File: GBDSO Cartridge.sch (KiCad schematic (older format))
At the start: 75 parts, among them J1 MJ-3523-SMT-TR, J2 MJ-3523-SMT-TR, J3 EdgeConnector, J5 Conn_01x02, J6 Conn_01x02, P1 100k, P2 100k, SW1 SW_SPDT, SW2 SW_SPDT, U1 TL072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

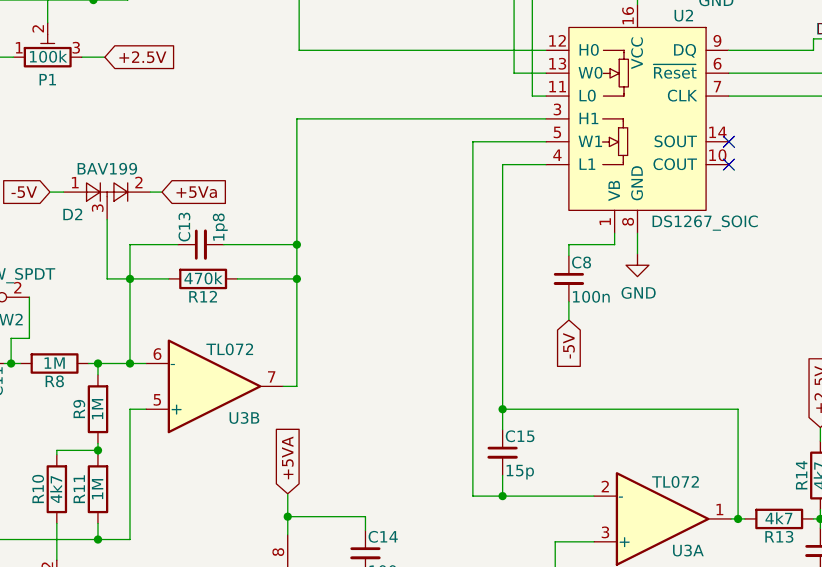
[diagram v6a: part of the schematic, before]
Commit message: issue #16, #17 and #18 are fixed in the schematic but not yet in the PCB
reopened issue #16 and #17 as they were not yet fixed in the PCB
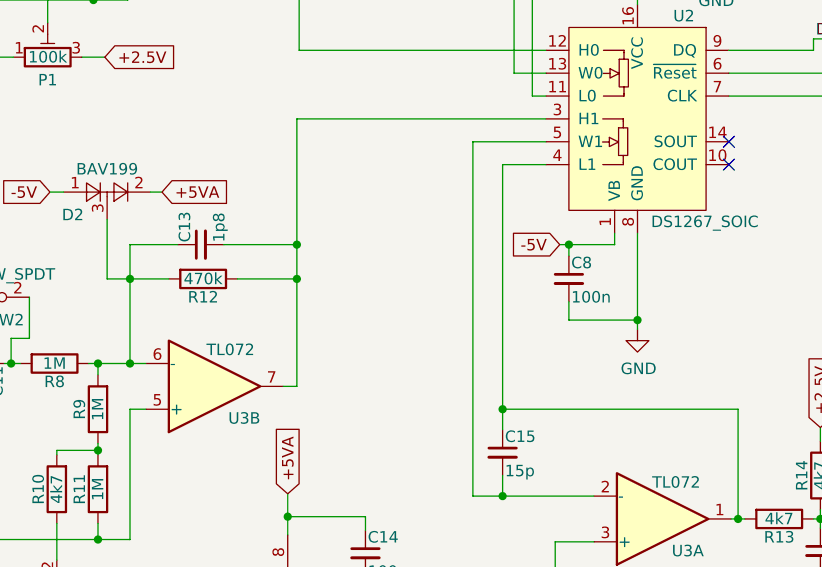
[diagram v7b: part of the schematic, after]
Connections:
- net +5Va is gone; now on net +5VA: D2.2
- net -5V: now also C8.1, U2.1 (VB); no longer C8.2
- net GND: now also C8.2
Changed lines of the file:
@@
 	1890 3310 1950 3310
 Text GLabel 2380 3310 2    50   Input ~ 0
-+5Va
++5VA
 Wire Wire Line
 	2380 3310 2330 3310
@@
 L power:GND #PWR0117
 U 1 1 5C828F4C
-P 4460 3580
-F 0 "#PWR0117" H 4460 3330 50  0001 C CNN
-F 1 "GND" H 4465 3407 50  0000 C CNN
-F 2 "" H 4460 3580 50  0001 C CNN
-F 3 "" H 4460 3580 50  0001 C CNN
-	1    4460 3580
-	1    0    0    -1
-$EndComp
-Wire Wire Line
-	4460 3580 4460 3490
+P 4460 3910
+F 0 "#PWR0117" H 4460 3660 50  0001 C CNN
+F 1 "GND" H 4465 3737 50  0000 C CNN
+F 2 "" H 4460 3910 50  0001 C CNN
+F 3 "" H 4460 3910 50  0001 C CNN
+	1    4460 3910
+	1    0    0    -1
+$EndComp
+Wire Wire Line
+	4460 3910 4460 3870
 Wire Wire Line
 	4360 3540 4160 3540
@@
 Wire Wire Line
 	4360 3490 4360 3540
-Text GLabel 4160 3870 3    50   Input ~ 0
+Text GLabel 4120 3540 0    50   Input ~ 0
 -5V
 Wire Wire Line
@@
 Wire Wire Line
 	5750 2500 5750 4860
+Wire Wire Line
+	4160 3540 4120 3540
+Connection ~ 4160 3540
+Wire Wire Line
+	4160 3870 4460 3870
 Wire Bus Line
 	5420 2660 5420 3300
@@
 Wire Bus Line
 	10200 3020 10200 6450
+Connection ~ 4460 3870
+Wire Wire Line
+	4460 3870 4460 3490
 $EndSCHEMATC

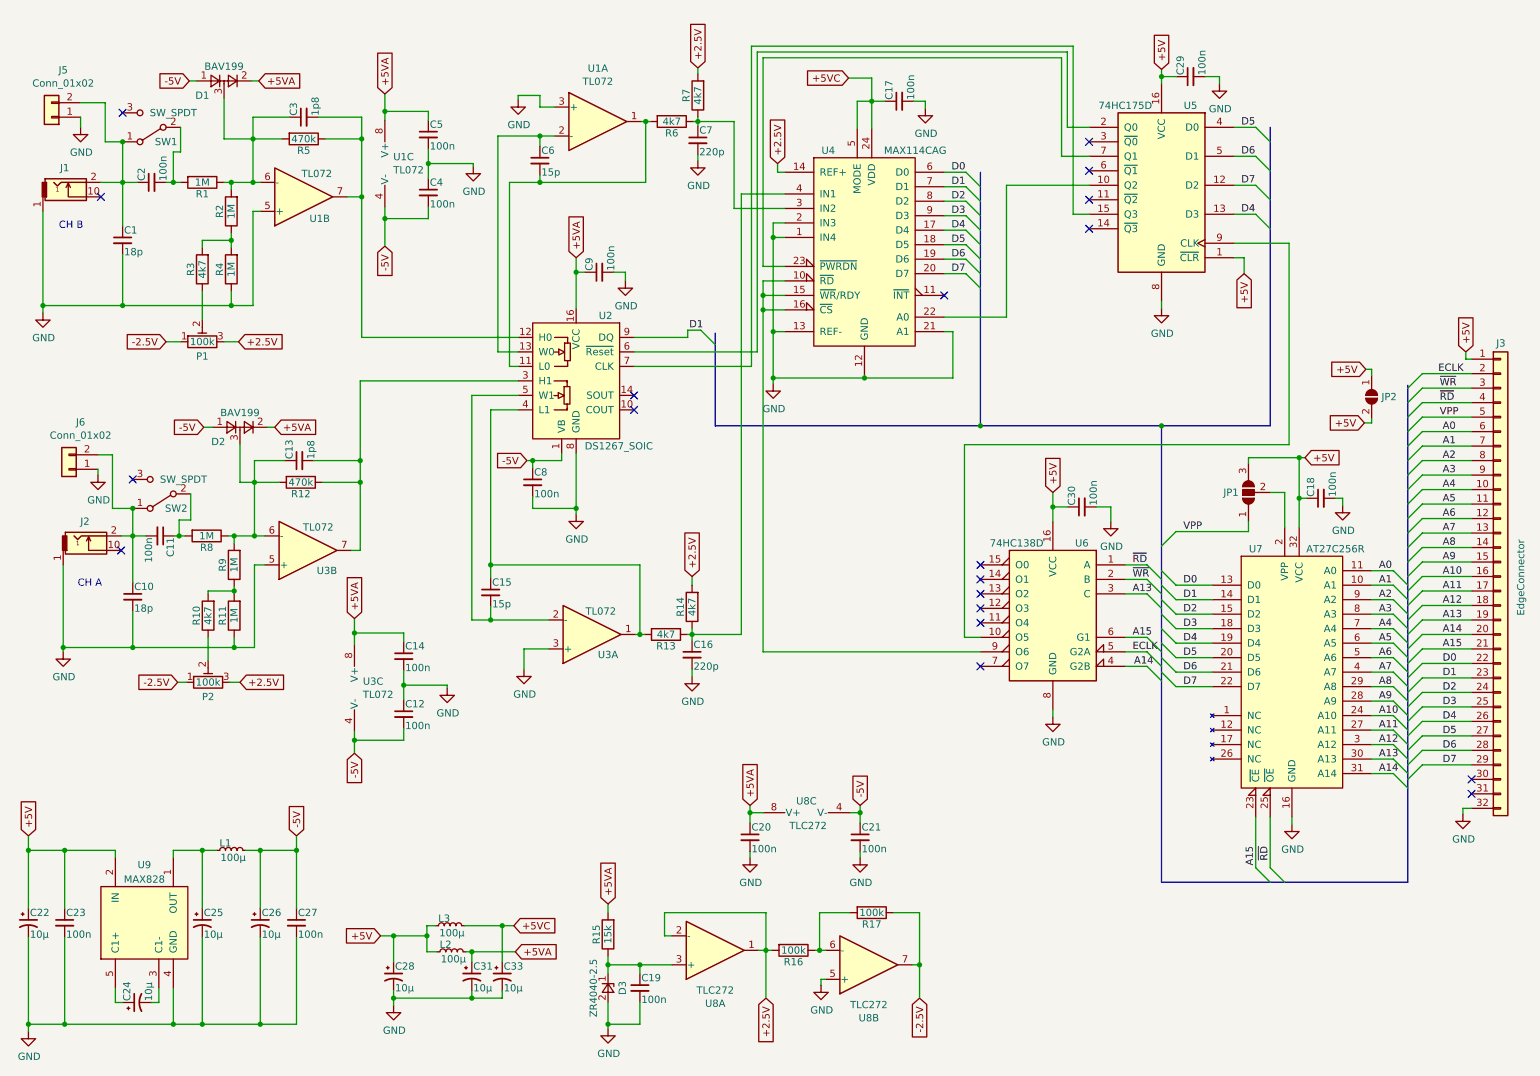
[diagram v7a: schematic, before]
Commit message: fix #16, fix #17, fix #18 in schematic and PCB
fixed issues #16,  #17, #18 in schematic and PCB, with improvement here and there.
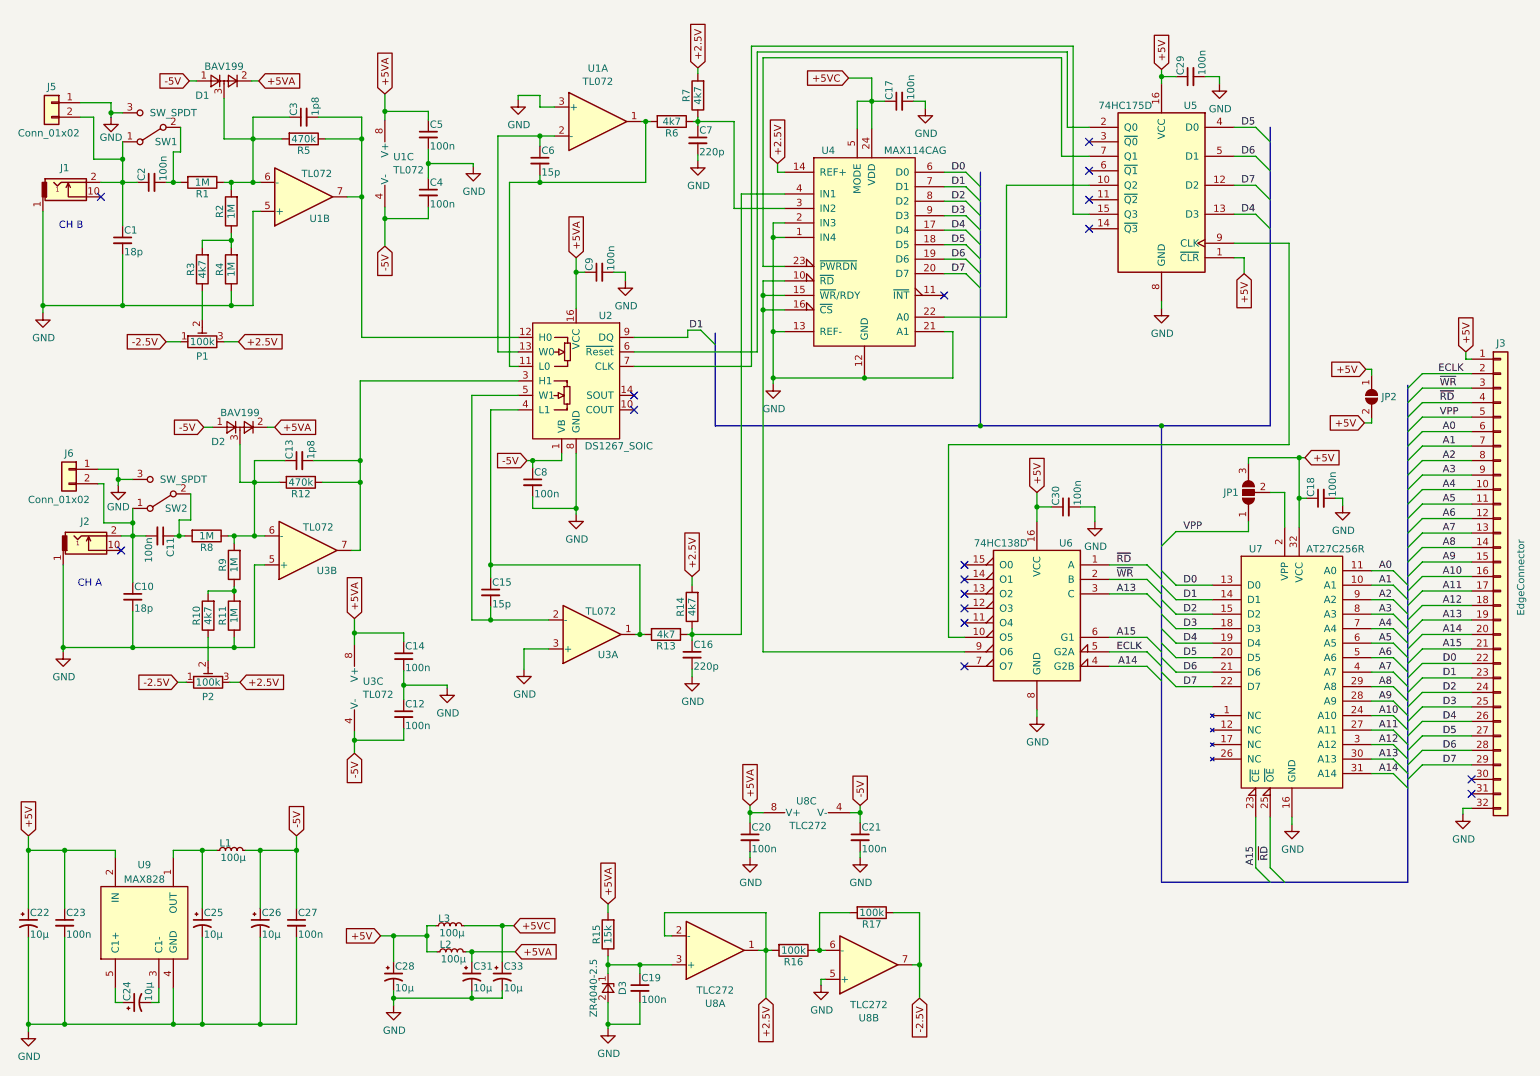
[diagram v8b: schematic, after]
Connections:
- net GND: now also SW1.3 (C), SW2.3 (C)
- no-connect marks 19 -> 17
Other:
- moved on the sheet: C30, J6, U6
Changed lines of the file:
@@
 L Device:C_Small C30
 U 1 1 5C828C55
-P 7950 3860
-F 0 "C30" H 7960 3930 50  0000 L CNN
-F 1 "100n" H 7960 3780 50  0000 L CNN
-F 2 "Capacitor_SMD:C_0805_2012Metric" H 7950 3860 50  0001 C CNN
-F 3 "" H 7950 3860 50  0001 C CNN
-	1    7950 3860
+P 7840 3860
+F 0 "C30" H 7850 3930 50  0000 L CNN
+F 1 "100n" H 7850 3780 50  0000 L CNN
+F 2 "Capacitor_SMD:C_0805_2012Metric" H 7840 3860 50  0001 C CNN
+F 3 "" H 7840 3860 50  0001 C CNN
+	1    7840 3860
 	0    -1   -1   0
 $EndComp
@@
 L 74HC138D:74HC138D U6
 U 1 1 5C828CE8
-P 7750 4610
-F 0 "U6" H 7550 5110 50  0000 C CNN
-F 1 "74HC138D" H 8000 5110 50  0000 C CNN
-F 2 "Package_SO:SOIC-16_3.9x9.9mm_P1.27mm" H 8600 4110 50  0001 C CNN
-F 3 "" H 7750 4610 50  0001 C CNN
-	1    7750 4610
+P 7640 4610
+F 0 "U6" H 7440 5110 50  0000 C CNN
+F 1 "74HC138D" H 7890 5110 50  0000 C CNN
+F 2 "Package_SO:SOIC-16_3.9x9.9mm_P1.27mm" H 8490 4110 50  0001 C CNN
+F 3 "" H 7640 4610 50  0001 C CNN
+	1    7640 4610
 	-1   0    0    -1
 $EndComp
@@
 L power:GND #PWR0102
 U 1 1 5C828D43
-P 7750 5310
-F 0 "#PWR0102" H 7750 5060 50  0001 C CNN
-F 1 "GND" H 7755 5137 50  0000 C CNN
-F 2 "" H 7750 5310 50  0001 C CNN
-F 3 "" H 7750 5310 50  0001 C CNN
-	1    7750 5310
-	1    0    0    -1
-$EndComp
-Wire Wire Line
-	7750 5310 7750 5260
+P 7640 5310
+F 0 "#PWR0102" H 7640 5060 50  0001 C CNN
+F 1 "GND" H 7645 5137 50  0000 C CNN
+F 2 "" H 7640 5310 50  0001 C CNN
+F 3 "" H 7640 5310 50  0001 C CNN
+	1    7640 5310
+	1    0    0    -1
+$EndComp
+Wire Wire Line
+	7640 5310 7640 5260
 $Comp
 L power:GND #PWR0103
@@
 Entry Wire Line
 	8400 4460 8500 4560
-Wire Wire Line
-	8400 4460 8250 4460
 Entry Wire Line
 	8400 4760 8500 4860
@@
 Entry Wire Line
 	8400 4960 8500 5060
-Wire Wire Line
-	8250 4760 8400 4760
-Wire Wire Line
-	8400 4860 8250 4860
-Wire Wire Line
-	8250 4960 8400 4960
-Text Label 8300 4460 0    50   ~ 0
+Text Label 8190 4460 0    50   ~ 0
 A13
-Text Label 8310 4960 0    50   ~ 0
+Text Label 8200 4960 0    50   ~ 0
 A14
-Text Label 8300 4860 0    50   ~ 0
+Text Label 8190 4860 0    50   ~ 0
 ECLK
-Text Label 8300 4760 0    50   ~ 0
+Text Label 8190 4760 0    50   ~ 0
 A15
 Entry Wire Line
@@
 Text Label 9250 6200 3    50   ~ 0
 ~RD
-Wire Wire Line
-	8250 4360 8400 4360
-Wire Wire Line
-	8250 4260 8400 4260
 Entry Wire Line
 	8400 4260 8500 4360
 Entry Wire Line
 	8400 4360 8500 4460
-Text Label 8300 4360 0    50   ~ 0
+Text Label 8190 4360 0    50   ~ 0
 ~WR
-Text Label 8300 4260 0    50   ~ 0
+Text Label 8190 4260 0    50   ~ 0
 ~RD
 $Comp
@@
 +5V
 Wire Wire Line
-	7850 3860 7750 3860
-Wire Wire Line
-	7750 3860 7750 3960
+	7740 3860 7640 3860
+Wire Wire Line
+	7640 3860 7640 3960
 $Comp
 L power:GND #PWR0107
 U 1 1 5C828E25
-P 8150 3960
-F 0 "#PWR0107" H 8150 3710 50  0001 C CNN
-F 1 "GND" H 8155 3787 50  0000 C CNN
-F 2 "" H 8150 3960 50  0001 C CNN
-F 3 "" H 8150 3960 50  0001 C CNN
-	1    8150 3960
-	1    0    0    -1
-$EndComp
-Wire Wire Line
-	8150 3960 8150 3860
-Wire Wire Line
-	8150 3860 8050 3860
-Text GLabel 7750 3760 1    50   Input ~ 0
+P 8040 3960
+F 0 "#PWR0107" H 8040 3710 50  0001 C CNN
+F 1 "GND" H 8045 3787 50  0000 C CNN
+F 2 "" H 8040 3960 50  0001 C CNN
+F 3 "" H 8040 3960 50  0001 C CNN
+	1    8040 3960
+	1    0    0    -1
+$EndComp
+Wire Wire Line
+	8040 3960 8040 3860
+Wire Wire Line
+	8040 3860 7940 3860
+Text GLabel 7640 3760 1    50   Input ~ 0
 +5V
 Wire Wire Line
-	7750 3760 7750 3860
-Connection ~ 7750 3860
+	7640 3760 7640 3860
+Connection ~ 7640 3860
 Text GLabel 8500 840  1    50   Input ~ 0
 +5V
@@
 	1680 1620 1730 1620
 Wire Wire Line
-	1330 1340 1330 1620
-Wire Wire Line
 	2100 4440 1920 4440
 Wire Wire Line
@@
 Connection ~ 920  4830
 Wire Wire Line
-	1400 3870 1400 4060
+	1400 3870 1400 3970
 Wire Wire Line
 	1800 3770 1800 3950
@@
 Connection ~ 5750 2400
 Wire Wire Line
-	5750 4860 7250 4860
+	5750 4860 7140 4860
 Connection ~ 5750 2500
 Wire Wire Line
-	7250 4760 7140 4760
-Wire Wire Line
-	7140 3430 9380 3430
+	7140 4760 7030 4760
+Wire Wire Line
+	7030 3430 9380 3430
 Wire Wire Line
 	9380 3430 9380 2040
@@
 NoConn ~ 8000 1740
 NoConn ~ 8000 1940
-NoConn ~ 7250 4960
-NoConn ~ 7250 4660
-NoConn ~ 7250 4560
-NoConn ~ 7250 4460
-NoConn ~ 7250 4360
-NoConn ~ 7250 4260
+NoConn ~ 7140 4960
+NoConn ~ 7140 4660
+NoConn ~ 7140 4560
+NoConn ~ 7140 4460
+NoConn ~ 7140 4360
+NoConn ~ 7140 4260
 $Comp
 L power:GND #PWR0117
@@
 Wire Wire Line
 	9950 2910 9950 2950
-NoConn ~ 1400 3670
-NoConn ~ 1330 1140
 $Comp
 L Connector_Generic:Conn_01x02 J5
 U 1 1 5CB7D891
-P 840 1170
-F 0 "J5" H 760 845 50  0000 C CNN
-F 1 "Conn_01x02" H 760 936 50  0000 C CNN
-F 2 "Connector_PinHeader_2.54mm:PinHeader_1x02_P2.54mm_Horizontal" H 840 1170 50  0001 C CNN
-F 3 "~" H 840 1170 50  0001 C CNN
-	1    840  1170
-	-1   0    0    1
+P 840 1070
+F 0 "J5" H 840 1180 50  0000 C CNN
+F 1 "Conn_01x02" H 860 860 50  0000 C CNN
+F 2 "Connector_PinHeader_2.54mm:PinHeader_1x02_P2.54mm_Horizontal" H 840 1070 50  0001 C CNN
+F 3 "~" H 840 1070 50  0001 C CNN
+	1    840  1070
+	-1   0    0    -1
 $EndComp
 $Comp
@@
 U 1 1 5CB7E2B7
 P 960 3600
-F 0 "J6" H 880 3275 50  0000 C CNN
-F 1 "Conn_01x02" H 880 3366 50  0000 C CNN
+F 0 "J6" H 960 3710 50  0000 C CNN
+F 1 "Conn_01x02" H 1030 3390 50  0000 C CNN
 F 2 "Connector_PinHeader_2.54mm:PinHeader_1x02_P2.54mm_Horizontal" H 960 3600 50  0001 C CNN
 F 3 "~" H 960 3600 50  0001 C CNN
 	1    960  3600
-	-1   0    0    1
-$EndComp
-Wire Wire Line
-	1400 3870 1260 3870
-Wire Wire Line
-	1260 3870 1260 3500
-Wire Wire Line
-	1260 3500 1160 3500
-Connection ~ 1400 3870
+	-1   0    0    -1
+$EndComp
 $Comp
 L power:GND #PWR0127
 U 1 1 5CBDB355
-P 1160 3640
-F 0 "#PWR0127" H 1160 3390 50  0001 C CNN
-F 1 "GND" H 1165 3467 50  0000 C CNN
-F 2 "" H 1160 3640 50  0001 C CNN
-F 3 "" H 1160 3640 50  0001 C CNN
-	1    1160 3640
-	1    0    0    -1
-$EndComp
-Wire Wire Line
-	1160 3600 1160 3640
-Wire Wire Line
-	1040 1070 1210 1070
-Wire Wire Line
-	1210 1070 1210 1340
-Wire Wire Line
-	1210 1340 1330 1340
-Connection ~ 1330 1340
+P 1300 3710
+F 0 "#PWR0127" H 1300 3460 50  0001 C CNN
+F 1 "GND" H 1300 3560 50  0000 C CNN
+F 2 "" H 1300 3710 50  0001 C CNN
+F 3 "" H 1300 3710 50  0001 C CNN
+	1    1300 3710
+	1    0    0    -1
+$EndComp
+Wire Wire Line
+	1130 1170 1130 1460
 $Comp
 L power:GND #PWR0128
 U 1 1 5CCF1BAC
-P 1040 1240
-F 0 "#PWR0128" H 1040 990 50  0001 C CNN
-F 1 "GND" H 1045 1067 50  0000 C CNN
-F 2 "" H 1040 1240 50  0001 C CNN
-F 3 "" H 1040 1240 50  0001 C CNN
-	1    1040 1240
-	1    0    0    -1
-$EndComp
-Wire Wire Line
-	1040 1170 1040 1240
+P 1250 1170
+F 0 "#PWR0128" H 1250 920 50  0001 C CNN
+F 1 "GND" H 1250 1030 50  0000 C CNN
+F 2 "" H 1250 1170 50  0001 C CNN
+F 3 "" H 1250 1170 50  0001 C CNN
+	1    1250 1170
+	1    0    0    -1
+$EndComp
 Text Notes 890  1950 0    50   ~ 0
 CH B
@@
 	3140 1130 3140 1190
 $Comp
-L power:GND #PWR?
+L power:GND #PWR0119
 U 1 1 5EA9683A
 P 3750 1510
-F 0 "#PWR?" H 3750 1260 50  0001 C CNN
+F 0 "#PWR0119" H 3750 1260 50  0001 C CNN
 F 1 "GND" H 3755 1337 50  0000 C CNN
 F 2 "" H 3750 1510 50  0001 C CNN
@@
 	2930 4730 2930 4810
 $Comp
-L power:GND #PWR?
+L power:GND #PWR0129
 U 1 1 5EBE7F77
 P 3570 5110
-F 0 "#PWR?" H 3570 4860 50  0001 C CNN
+F 0 "#PWR0129" H 3570 4860 50  0001 C CNN
 F 1 "GND" H 3575 4937 50  0000 C CNN
 F 2 "" H 3570 5110 50  0001 C CNN
@@
 	6340 900  6500 900
 Wire Wire Line
-	7140 3430 7140 4760
+	7030 3430 7030 4760
 Wire Wire Line
 	5750 2500 5750 4860
@@
 Wire Wire Line
 	4160 3870 4460 3870
+Connection ~ 4460 3870
+Wire Wire Line
+	4460 3870 4460 3490
+Wire Wire Line
+	8140 4260 8400 4260
+Wire Wire Line
+	8140 4360 8400 4360
+Wire Wire Line
+	8140 4460 8400 4460
+Wire Wire Line
+	8140 4760 8400 4760
+Wire Wire Line
+	8140 4860 8400 4860
+Wire Wire Line
+	8140 4960 8400 4960
+Wire Wire Line
+	1250 1170 1250 1140
+Wire Wire Line
+	1250 1140 1330 1140
+Wire Wire Line
+	1130 1170 1040 1170
+Wire Wire Line
+	1250 1070 1250 1140
+Wire Wire Line
+	1040 1070 1250 1070
+Connection ~ 1250 1140
+Wire Wire Line
+	1130 1460 1330 1460
+Wire Wire Line
+	1330 1340 1330 1460
+Connection ~ 1330 1460
+Wire Wire Line
+	1330 1460 1330 1620
+Wire Wire Line
+	1400 3970 1200 3970
+Wire Wire Line
+	1200 3970 1200 3700
+Wire Wire Line
+	1200 3700 1160 3700
+Connection ~ 1400 3970
+Wire Wire Line
+	1400 3970 1400 4060
+Wire Wire Line
+	1160 3600 1300 3600
+Wire Wire Line
+	1300 3600 1300 3670
+Connection ~ 1300 3670
+Wire Wire Line
+	1300 3670 1300 3710
+Wire Wire Line
+	1300 3670 1400 3670
 Wire Bus Line
 	5420 2660 5420 3300
@@
 Wire Bus Line
 	10200 3020 10200 6450
-Connection ~ 4460 3870
-Wire Wire Line
-	4460 3870 4460 3490
 $EndSCHEMATC
